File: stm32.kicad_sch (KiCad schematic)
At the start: 69 parts, among them IC1 LTC3621EMS8E-3.3#PBF, J1 TC2030, J2 USB_C_Receptacle_PowerOnly_6P, J3 Conn_01x02, J4 Conn_01x02, J5 Conn_01x03, Q1 DMG2305UX, Q2 FS8205A, SW1 SW_Push, SW2 SW_Push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

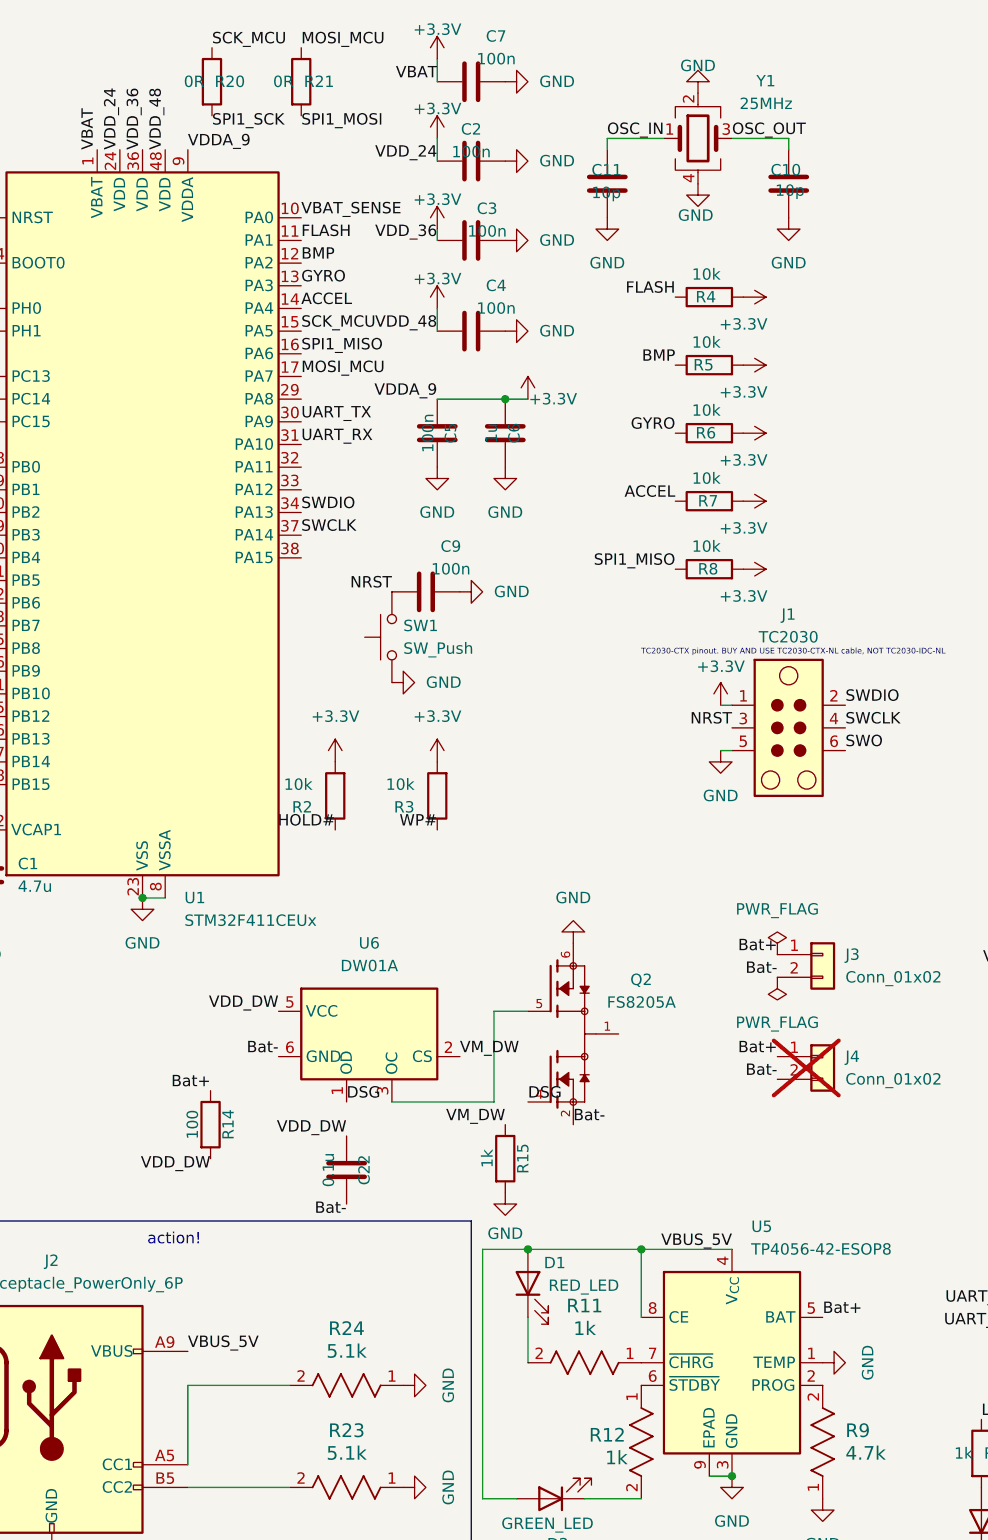
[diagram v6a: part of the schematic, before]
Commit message: Resolve ERC: fix +3.3V power flag, FS8205 drain no-connect
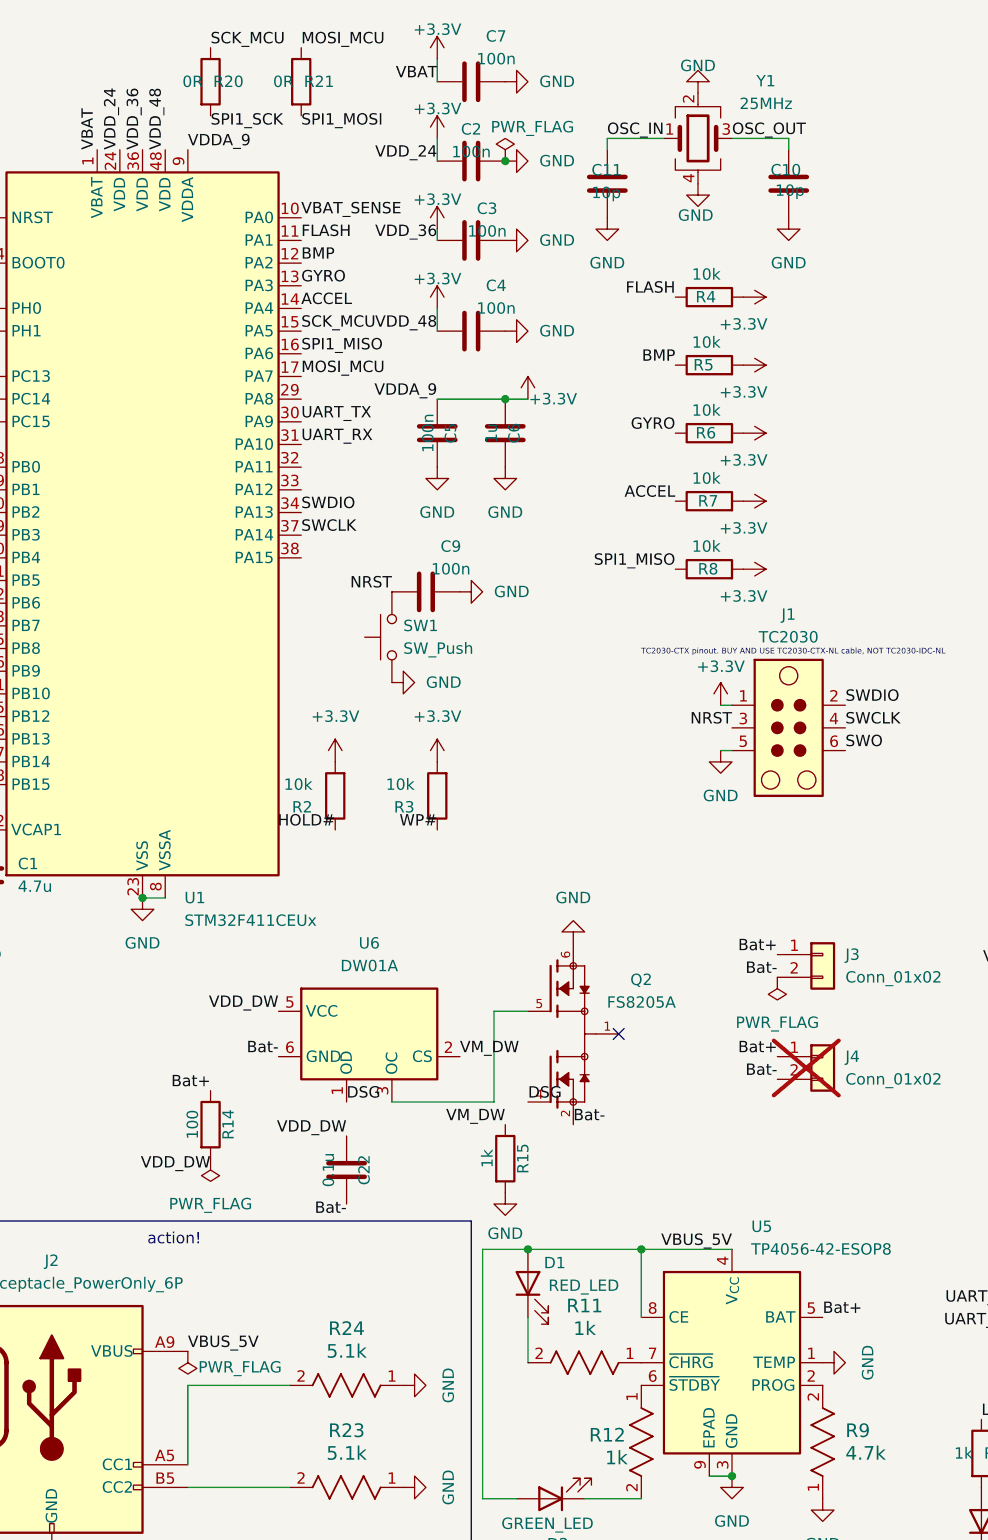
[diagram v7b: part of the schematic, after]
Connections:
- no-connect marks 4 -> 5
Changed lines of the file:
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@@
 	)
 	(junction
+		(at 82.55 27.94)
+		(diameter 0)
+		(color 0 0 0 0)
+	)
+	(junction
 		(at 85.09 149.86)
 		(diameter 0)
@@
 	)
 	(no_connect
+		(at 95.25 125.73)
+	)
+	(no_connect
 		(at 193.04 48.26)
 	)
@@
 	)
 	(label "SCK_MCU"
-		(at 49.69 15.24 0)
+		(at 49.53 15.24 0)
 		(effects
 			(font
@@
 	)
 	(label "SPI1_SCK"
-		(at 49.69 22.86 0)
+		(at 49.53 22.86 0)
 		(effects
 			(font
@@
 	)
 	(symbol
+		(lib_id "power:PWR_FLAG")
+		(at 49.53 139.7 180)
+		(unit 1)
+		(exclude_from_sim no)
+		(in_bom yes)
+		(on_board yes)
+		(dnp no)
+		(fields_autoplaced yes)
+		(property "Reference" "#FLG03"
+			(at 49.53 141.605 0)
+			(effects
+				(font
+					(size 1.27 1.27)
+				)
+				(hide yes)
+			)
+		)
+		(property "Value" "PWR_FLAG"
+			(at 49.53 144.78 0)
+			(effects
+				(font
+					(size 1.27 1.27)
+				)
+			)
+		)
+		(property "Footprint" ""
+			(at 49.53 139.7 0)
+			(effects
+				(font
+					(size 1.27 1.27)
+				)
+				(hide yes)
+			)
+		)
+		(property "Datasheet" "~"
+			(at 49.53 139.7 0)
+			(effects
+				(font
+					(size 1.27 1.27)
+				)
+				(hide yes)
+			)
+		)
+		(property "Description" "Special symbol for telling ERC where power comes from"
+			(at 49.53 139.7 0)
+			(effects
+				(font
+					(size 1.27 1.27)
+				)
+				(hide yes)
+			)
+		)
+		(pin "1"
+		)
+		(instances
+			(project "stm32"
+				(path "/807257e6-524f-404b-b91f-049b9c2bdd5b"
+					(reference "#FLG03")
+					(unit 1)
+				)
+			)
+		)
+	)
+	(symbol
 		(lib_id "power:+3.3V")
 		(at 74.93 95.25 0)
@@
 	(symbol
 		(lib_id "power:PWR_FLAG")
-		(at 113.03 116.84 0)
+		(at 82.55 27.94 0)
+		(unit 1)
+		(exclude_from_sim no)
+		(in_bom yes)
+		(on_board yes)
+		(dnp no)
+		(property "Reference" "#FLG04"
+			(at 82.55 26.035 0)
+			(effects
+				(font
+					(size 1.27 1.27)
+				)
+				(hide yes)
+			)
+		)
+		(property "Value" "PWR_FLAG"
+			(at 85.598 24.13 0)
+			(effects
+				(font
+					(size 1.27 1.27)
+				)
+			)
+		)
+		(property "Footprint" ""
+			(at 82.55 27.94 0)
+			(effects
+				(font
+					(size 1.27 1.27)
+				)
+				(hide yes)
+			)
+		)
+		(property "Datasheet" "~"
+			(at 82.55 27.94 0)
+			(effects
+				(font
+					(size 1.27 1.27)
+				)
+				(hide yes)
+			)
+		)
+		(property "Description" "Special symbol for telling ERC where power comes from"
+			(at 82.55 27.94 0)
+			(effects
+				(font
+					(size 1.27 1.27)
+				)
+				(hide yes)
+			)
+		)
+		(pin "1"
+		)
+		(instances
+			(project "stm32"
+				(path "/807257e6-524f-404b-b91f-049b9c2bdd5b"
+					(reference "#FLG04")
+					(unit 1)
+				)
+			)
+		)
+	)
+	(symbol
+		(lib_id "power:PWR_FLAG")
+		(at 46.99 161.29 180)
 		(unit 1)
 		(exclude_from_sim no)
@@
 		(on_board yes)
 		(dnp no)
-		(fields_autoplaced yes)
 		(property "Reference" "#FLG01"
-			(at 113.03 114.935 0)
+			(at 46.99 163.195 0)
 			(effects
 				(font
@@
 		)
 		(property "Value" "PWR_FLAG"
-			(at 113.03 111.76 0)
+			(at 52.832 163.068 0)
 			(effects
 				(font
@@
 		)
 		(property "Footprint" ""
-			(at 113.03 116.84 0)
+			(at 46.99 161.29 0)
 			(effects
 				(font
@@
 		)
 		(property "Datasheet" "~"
-			(at 113.03 116.84 0)
+			(at 46.99 161.29 0)
 			(effects
 				(font
@@
 		)
 		(property "Description" "Special symbol for telling ERC where power comes from"
-			(at 113.03 116.84 0)
+			(at 46.99 161.29 0)
 			(effects
 				(font
@@
 		)
 		(instances
-			(project ""
+			(project "stm32"
 				(path "/807257e6-524f-404b-b91f-049b9c2bdd5b"
 					(reference "#FLG01")
@@
 	(symbol
 		(lib_id "Device:R")
-		(at 49.69 19.05 0)
+		(at 49.53 19.05 0)
 		(unit 1)
 		(exclude_from_sim no)
@@
 		(dnp no)
 		(property "Reference" "R20"
-			(at 51.69 19.05 0)
+			(at 51.53 19.05 0)
 			(effects
 				(font
@@
 		)
 		(property "Value" "0R"
-			(at 47.69 19.05 0)
+			(at 47.53 19.05 0)
 			(effects
 				(font
@@
 		)
 		(property "Footprint" "Resistor_SMD:R_0402_1005Metric"
-			(at 49.69 19.05 90)
+			(at 49.53 19.05 90)
 			(effects
 				(font
@@
 		)
 		(property "Datasheet" "~"
-			(at 49.69 19.05 0)
+			(at 49.53 19.05 0)
 			(effects
 				(font
@@
 		)
 		(property "Description" "Resistor"
-			(at 49.69 19.05 0)
+			(at 49.53 19.05 0)
 			(effects
 				(font

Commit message: Assign J5 UART header footprint; import netlist to PCB for layout
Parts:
- J5: footprint (none) -> Connector_PinHeader_2.54mm:PinHeader_1x03_P2.54mm_Vertical
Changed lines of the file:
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@@
 			)
 		)
-		(property "Footprint" ""
+		(property "Footprint" "Connector_PinHeader_2.54mm:PinHeader_1x03_P2.54mm_Vertical"
 			(at 144.78 158.75 0)
 			(effects
